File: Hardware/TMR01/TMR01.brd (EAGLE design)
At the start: 100 x 80 mm, 38 parts, among them U1 ATMEGA328P_TQFP, U2 DS3234

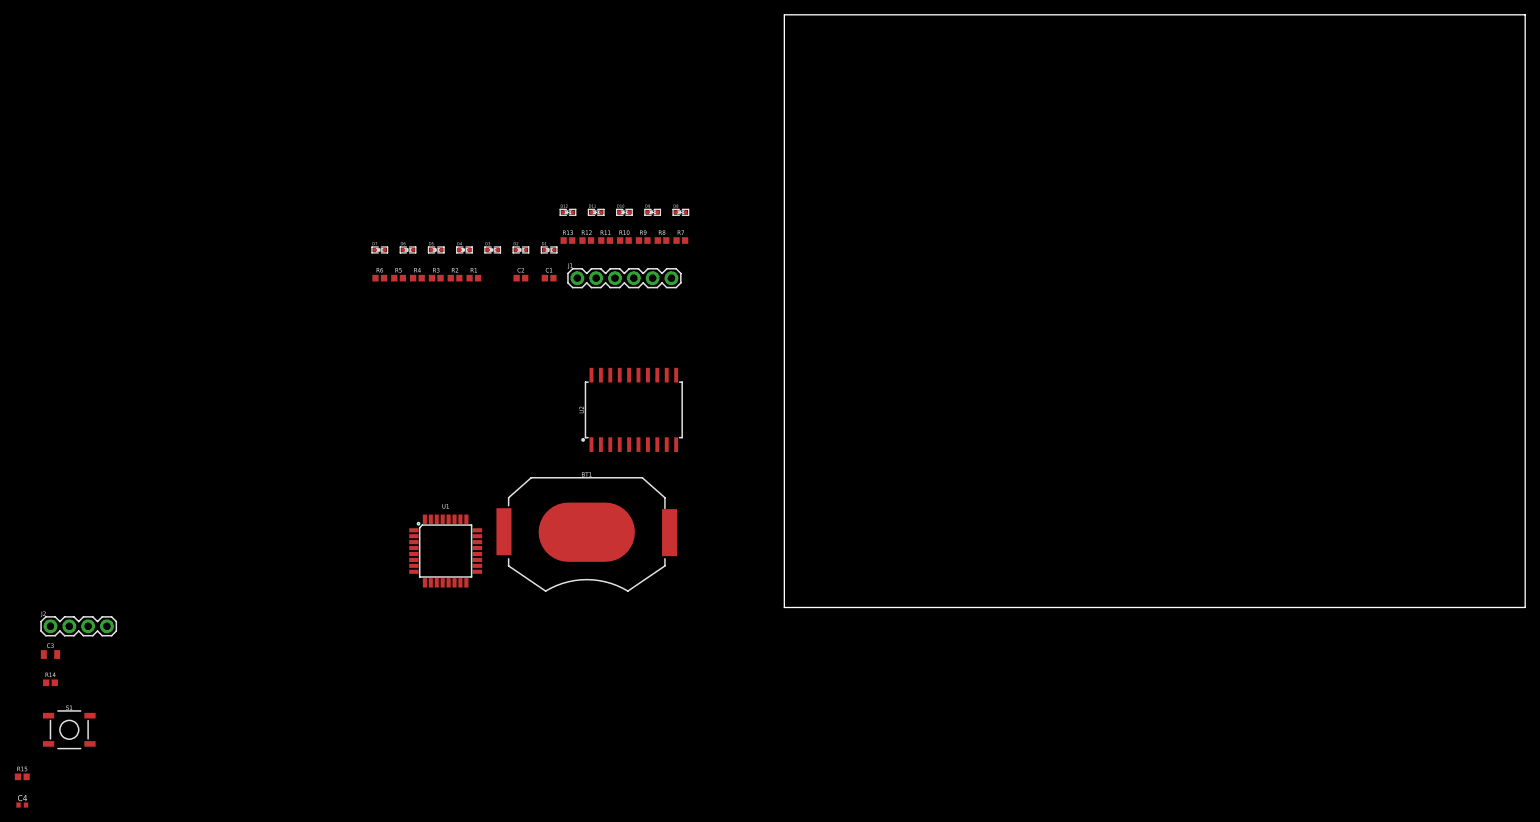
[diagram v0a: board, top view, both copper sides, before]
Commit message: Board created with a watch layout
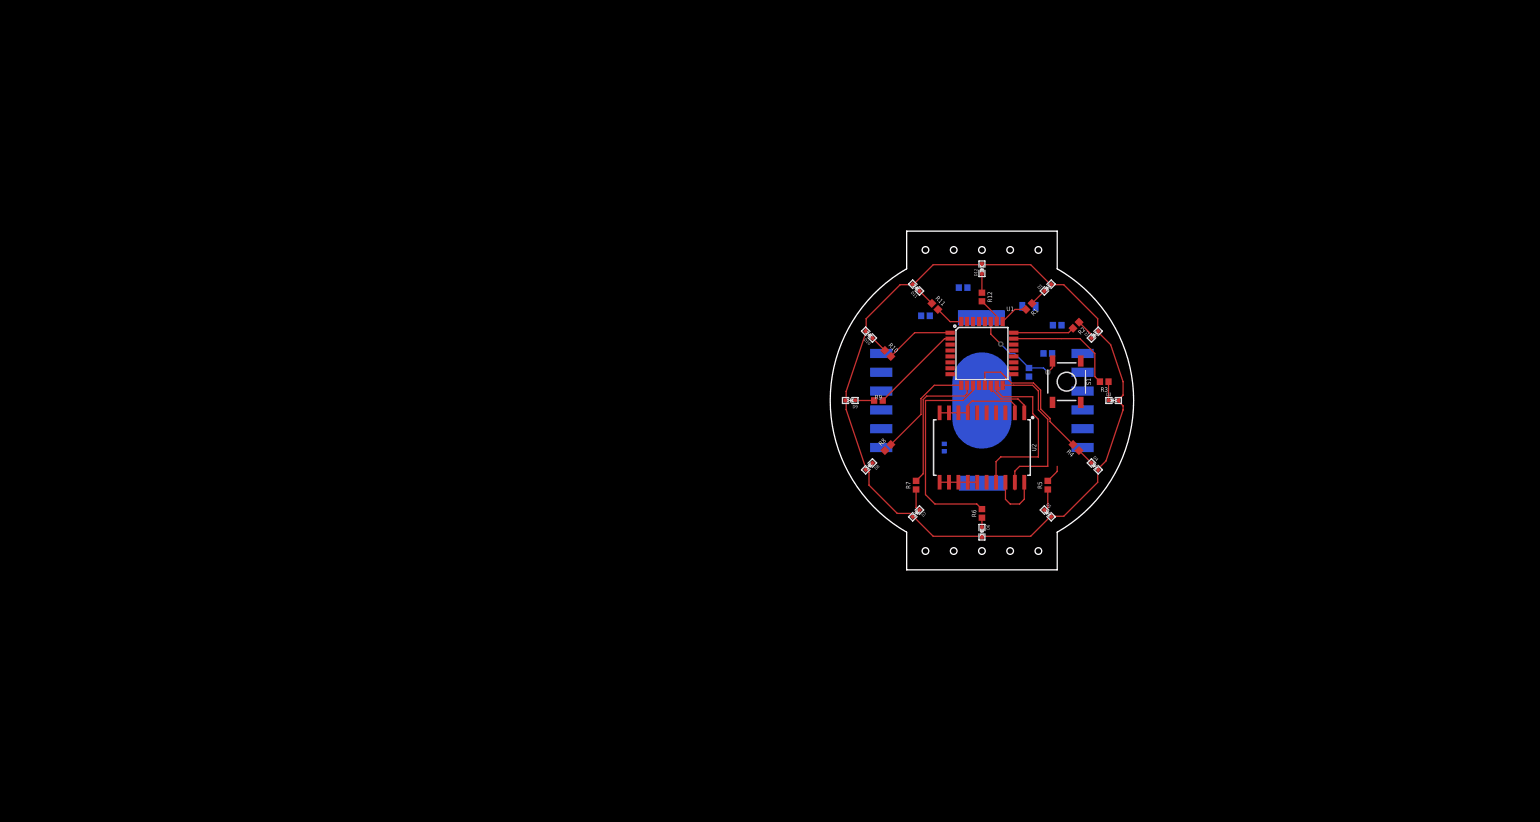
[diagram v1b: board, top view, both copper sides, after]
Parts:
- J1: device SparkFun-Connectors:1X06 -> SparkFun-Connectors:1X06-SMD-FEMALE
- J2: device SparkFun-Connectors:1X04 -> SparkFun-Connectors:1X06-SMD-FEMALE
- moved R15 149.8 mm to (35.6, 34.3), flipped to the bottom, turned to 180 degrees
- moved S1 142.6 mm to (38.1, 30.5), turned to 270 degrees
- moved C3 140.2 mm to (33.0, 40.6), flipped to the bottom
- moved J2 139.3 mm to (36.8, 27.9), flipped to the bottom, turned to 90 degrees
- moved R14 138.6 mm to (33.0, 31.8), flipped to the bottom, turned to 270 degrees
- moved C4 133.5 mm to (21.6, 21.6), flipped to the bottom, turned to 90 degrees
- moved FRAME1 96.2 mm to (8.89, -2.54)
- moved R5 92.0 mm to (35.6, 16.5), turned to 90 degrees
- moved R4 91.8 mm to (39.4, 21.6), turned to 135 degrees
- moved R3 91.2 mm to (43.2, 30.5), turned to 180 degrees
- moved D4 90.0 mm to (41.9, 19.1), turned to 315 degrees
- moved D5 89.9 mm to (35.6, 12.7), turned to 315 degrees
- moved R6 87.3 mm to (26.7, 12.7), turned to 90 degrees
- moved D6 86.3 mm to (26.7, 10.2), turned to 270 degrees
- moved D3 86.2 mm to (44.5, 27.9)
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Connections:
- removed net N$10: R2.2
- removed net N$11: R3.2
- removed net N$12: R4.2
- removed net N$13: R5.2
- removed net N$14: R6.2
- removed net N$15: R7.2
- removed net N$16: R8.2
- removed net N$19: R9.2
- removed net N$21: R10.2
- removed net N$23: R11.2
- removed net N$25: R12.2
- removed net N$26: R15.2, U2.5
- removed net N$28: U1.14
- removed net N$29: U1.13
- removed net N$30: U1.12
- removed net N$33: U1.32
- removed net N$34: U1.1
- removed net N$35: U1.2
- removed net N$36: U1.9
- removed net N$37: U1.10
- removed net N$38: U1.11
- removed net N$40: U2.1
- removed net N$9: R1.2
- new net D1: R11.2, U1.32
- new net D10: R2.2, U1.24
- new net D11: R1.2, U1.25
- new net D12: R12.2, U1.26
- new net D2: R10.2, U1.1
- new net D3: R9.2, U1.2
- new net D4: R8.2, U1.9
- new net D5: R7.2, U1.10
- new net D6: R6.2, U1.11
- new net D7: R5.2, U1.12
- new net D8: R4.2, U1.13
- new net D9: R3.2, U1.23
- new net SQW: J2.1, R15.2, U2.5
- new net SS: J2.2, U1.14, U2.1
- net MISO: now also J2.5; no longer J2.3
- net MOSI: now also J2.4; no longer J2.2
- net PUSH: now also U1.27
- net RST: now also J2.3; no longer J2.1
- net SCK: now also J2.6; no longer J2.4
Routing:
- net GND: track 0.00 -> 139.9 mm
- net D6: track 0.00 -> 28.8 mm
- net MOSI: track 0.00 -> 24.0 mm
- net MISO: track 0.00 -> 23.1 mm
- net D8: track 0.00 -> 19.4 mm
- net D5: track 0.00 -> 18.7 mm
- net D9: track 0.00 -> 15.9 mm
- net D4: track 0.00 -> 14.1 mm
- net PUSH: track 0.00 -> 13.3 mm, vias 0 -> 2
- net D3: track 0.00 -> 12.6 mm
- net D2: track 0.00 -> 9.33 mm
- net D10: track 0.00 -> 8.25 mm
- net SCK: track 0.00 -> 7.67 mm
- net SS: track 0.00 -> 7.08 mm
- net D1: track 0.00 -> 3.82 mm
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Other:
- board size 100 x 80 mm -> 41 x 45.7 mm

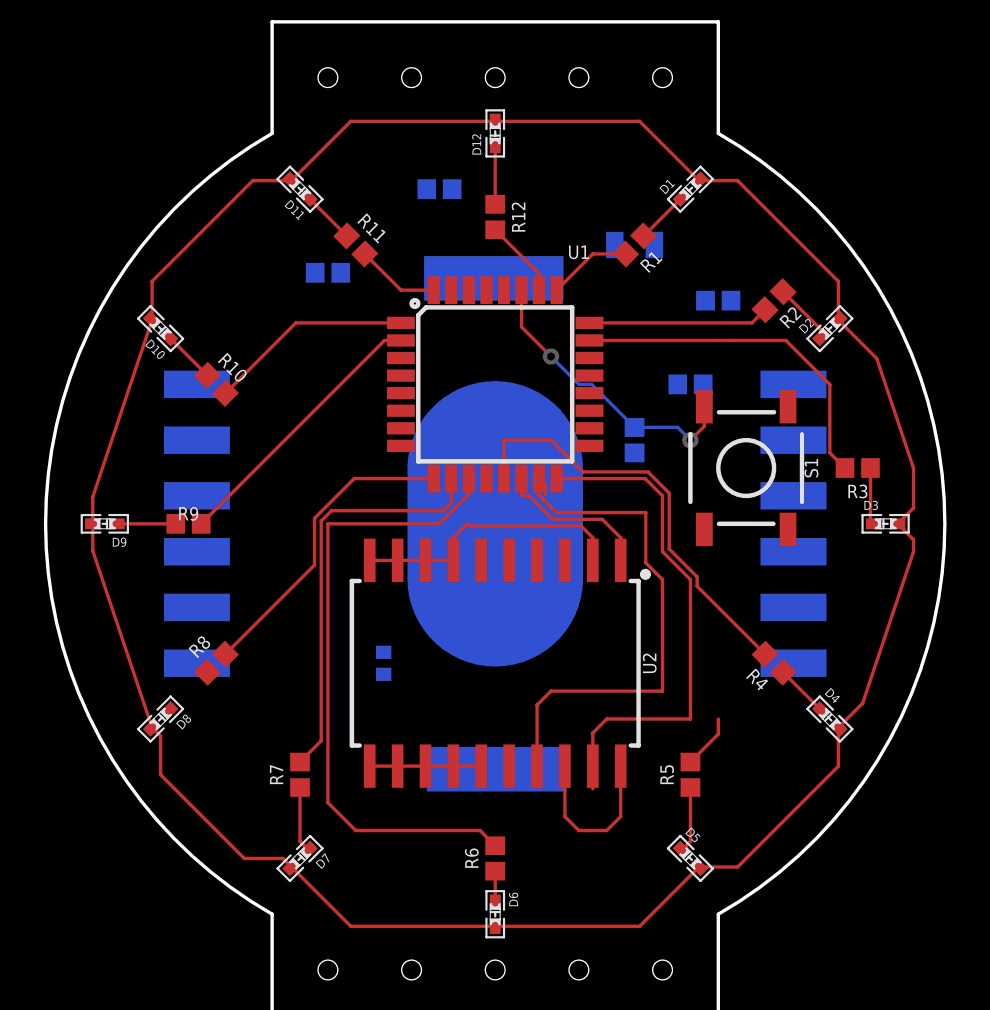
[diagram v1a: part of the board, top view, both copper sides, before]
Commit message: connecting grounds and vcc with via
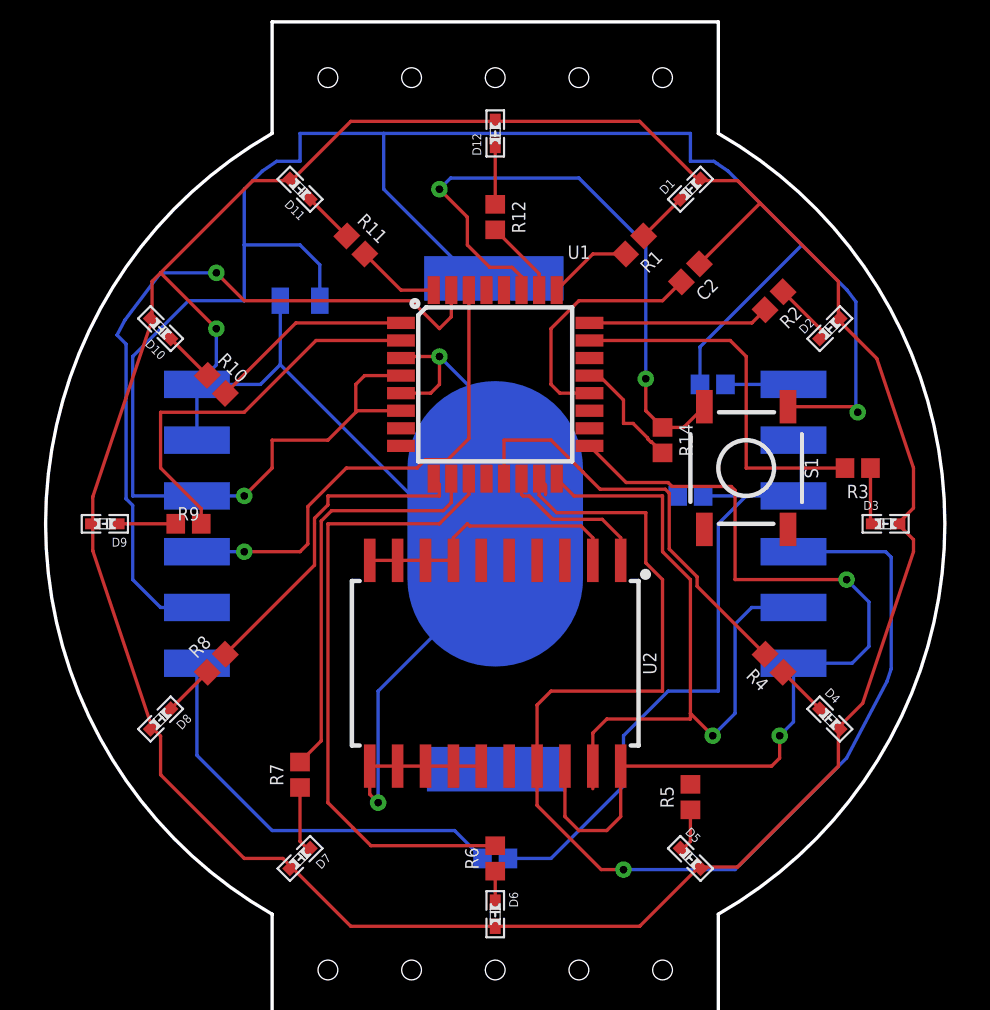
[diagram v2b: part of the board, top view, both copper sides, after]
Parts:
- removed C4: 22pF, Perfect_0402:0402
- moved C1 27.7 mm to (26.7, 12.7), turned to 180 degrees
- moved R13 18.1 mm to (35.6, 29.2), turned to 180 degrees
- moved C3 15.5 mm to (17.8, 38.1), turned to 180 degrees
- moved C2 1.80 mm to (35.6, 39.4), flipped to the top, turned to 225 degrees
- moved R14 1.27 mm to (34.3, 31.8), flipped to the top
- moved R5 1.02 mm to (35.6, 15.5)
- moved R15 1.02 mm to (36.6, 34.3)
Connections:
- net GND: no longer C4.2
- net VCC: no longer C4.1
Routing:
- net VCC: track 0.00 -> 102.4 mm, vias 0 -> 2
- net GND: track 139.9 -> 208.4 mm, vias 0 -> 3
- net SCK: track 7.67 -> 43.5 mm, vias 0 -> 2
- net TX: track 0.00 -> 34.1 mm, vias 0 -> 1
- net MOSI: track 24.0 -> 57.4 mm, vias 0 -> 1
- net RST: track 0.00 -> 27.6 mm
- net RX: track 0.00 -> 22.3 mm, vias 0 -> 1
- net DTR: track 0.00 -> 19.1 mm
- net PUSH: track 13.3 -> 29.0 mm
- net N$17: track 0.00 -> 11.3 mm
- net MISO: track 23.1 -> 33.0 mm, vias 0 -> 1
- net D3: track 12.6 -> 18.1 mm
- net SQW: track 0.00 -> 3.10 mm
- net D7: track 2.49 -> 0.00 mm
- net N$1: track 0.00 -> 2.46 mm
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
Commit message: everything except D7
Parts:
- removed R15: 10k, SparkFun-Resistors:0402
- J2: device SparkFun-Connectors:1X06-SMD-FEMALE -> SparkFun-Connectors:1X04_SMD_RA_FEMALE
- moved R13 6.48 mm to (36.8, 35.6), turned to 270 degrees
- moved J2 3.81 mm to (33.0, 27.9)
- moved R3 1.27 mm to (44.5, 30.5), turned to 90 degrees
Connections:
- removed net SQW: J2.1, R15.2, U2.5
- net MISO: now also J2.3; no longer J2.5
- net MOSI: now also J2.2; no longer J2.4
- net RST: now also J2.1; no longer J2.3
- net SCK: now also J2.4; no longer J2.6
- net SS: no longer J2.2
- net VCC: no longer R15.1
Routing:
- net VCC: track 102.4 -> 173.7 mm, vias 2 -> 6
- net RST: track 27.6 -> 65.8 mm, vias 0 -> 1
- net MISO: track 33.0 -> 44.4 mm
- net D6: track 28.8 -> 35.7 mm
- net N$17: track 11.3 -> 16.4 mm
- net GND: track 208.4 -> 204.3 mm, vias 3 -> 4
- net SQW: track 3.10 -> 0.00 mm
- net MOSI: track 57.4 -> 59.1 mm
- net SCK: track 43.5 -> 45.0 mm, vias 2 -> 3
- net D9: track 17.0 -> 18.3 mm
- net DTR: track 19.1 -> 19.9 mm
